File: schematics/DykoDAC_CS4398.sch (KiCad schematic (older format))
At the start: 14 parts, among them U7 CS4398

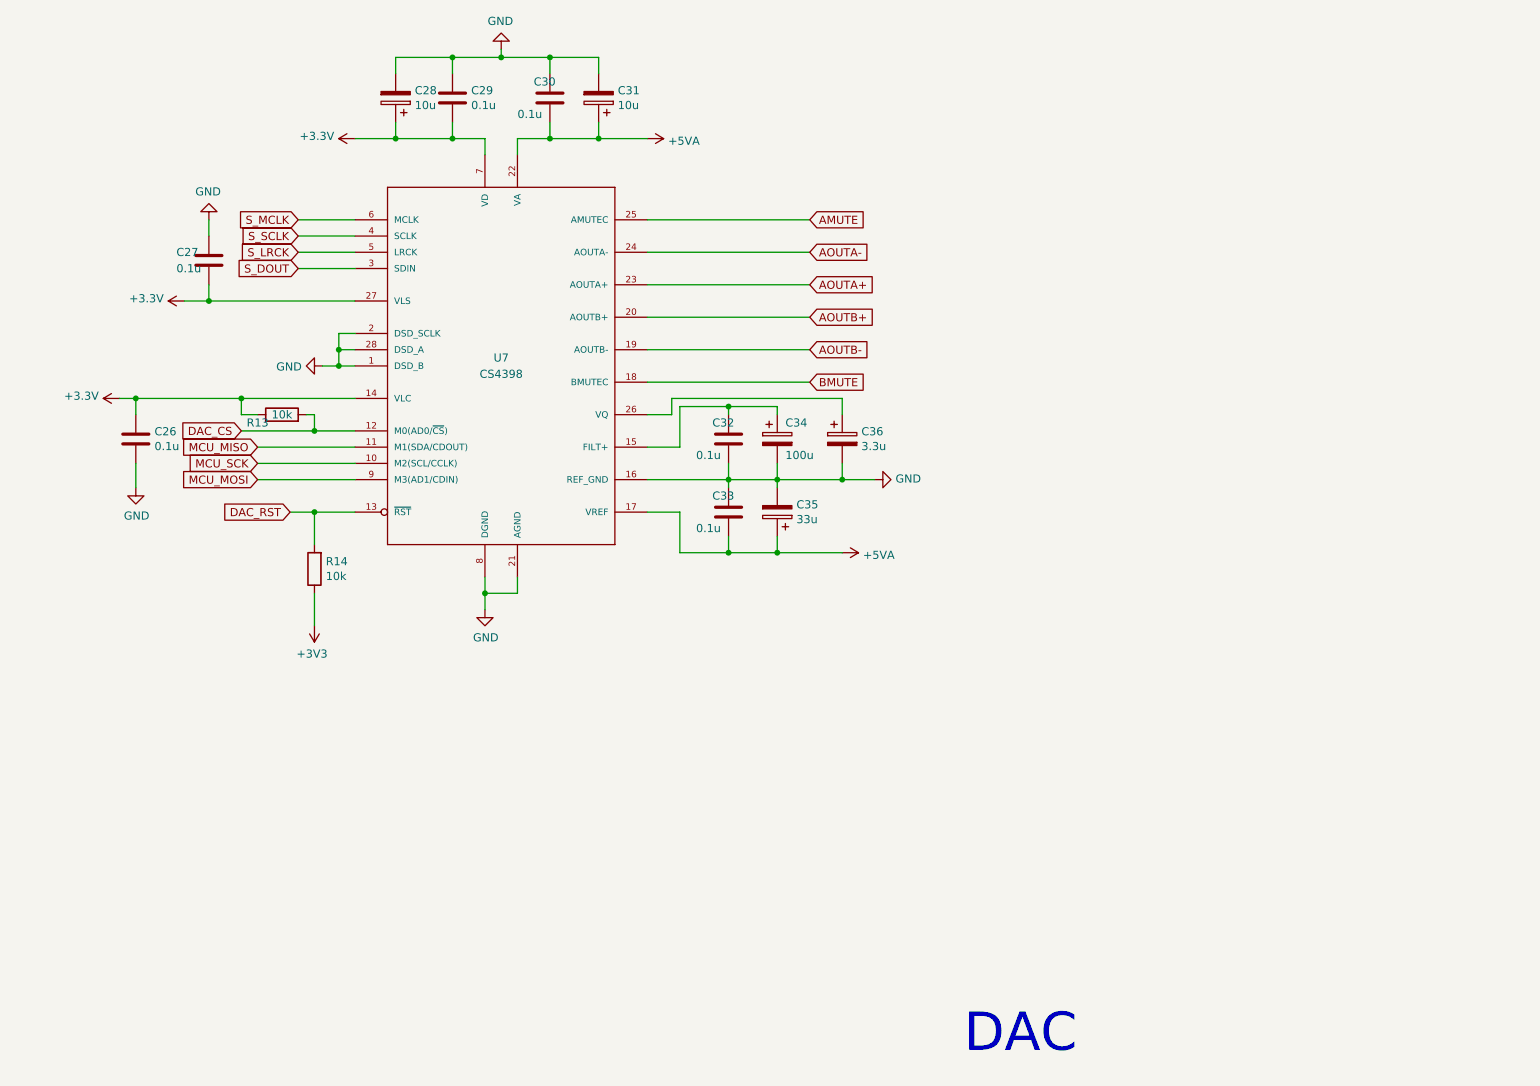
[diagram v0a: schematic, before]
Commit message: mcu input and usb added, oscilators moved to DAC schematics
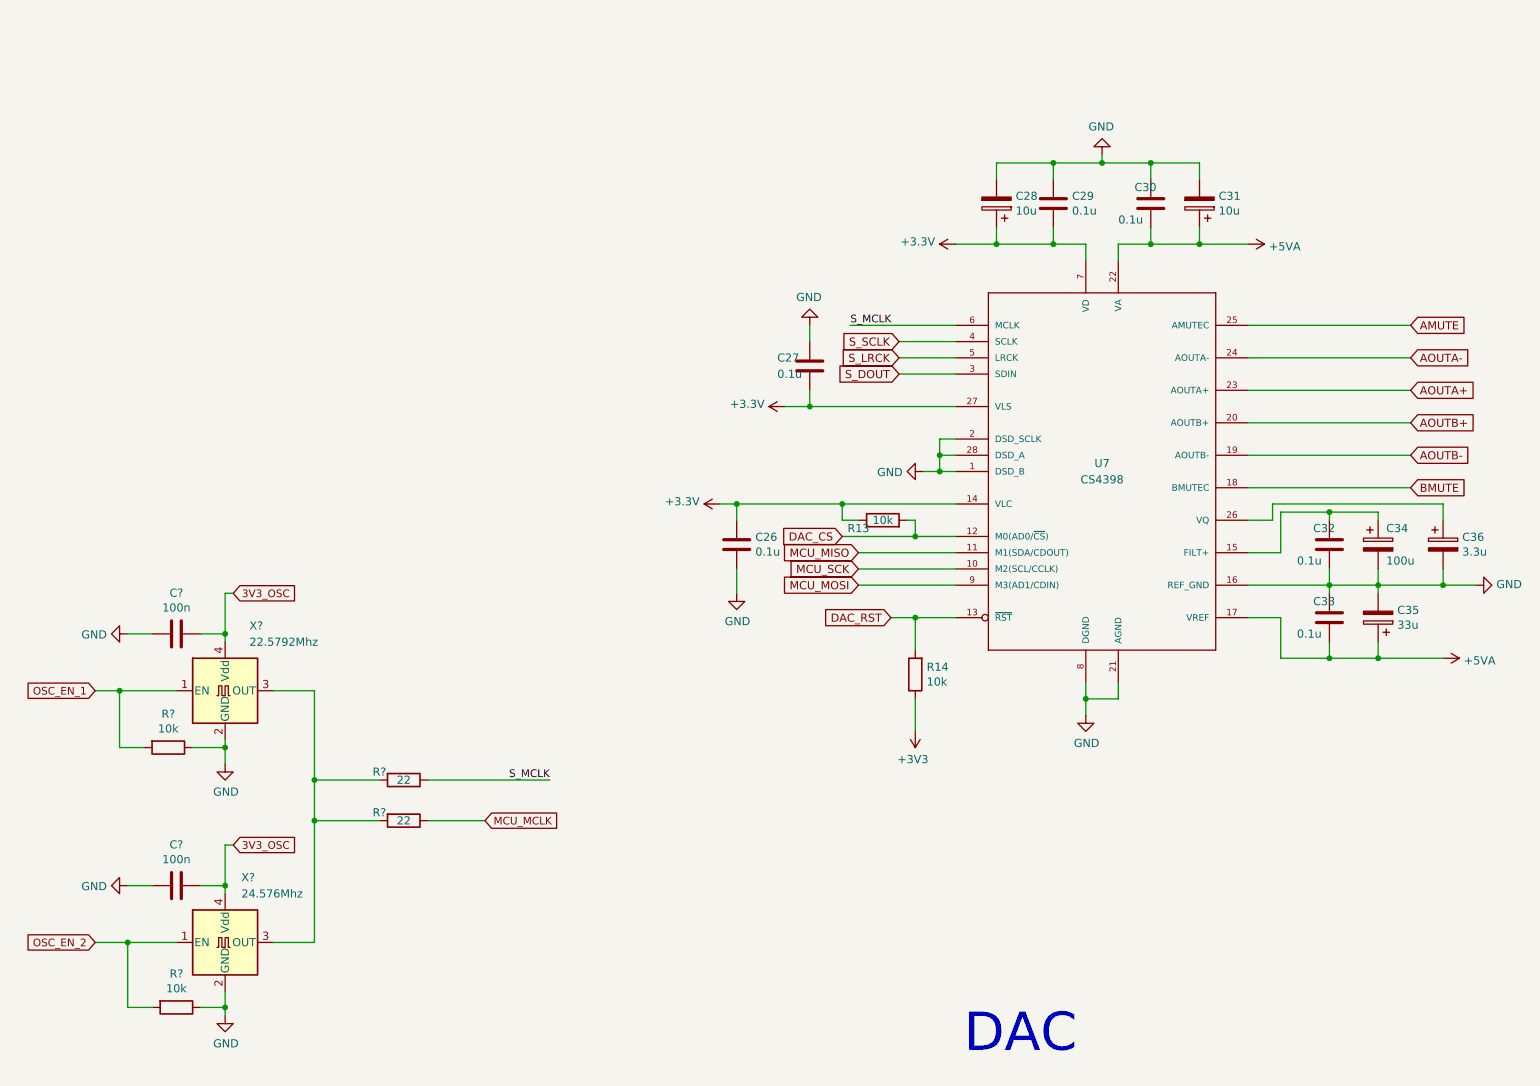
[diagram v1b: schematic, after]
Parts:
- added C? (x2): 100n, symbol Device:C
- added R? (x2): 22, symbol Device:R
- added R? (x2): 10k, symbol Device:R
- added X?: 22.5792Mhz, Oscillator:Oscillator_SMD_TXC_7C-4Pin_5.0x3.2mm, symbol Oscillator:TXC-7C
- added X?: 24.576Mhz, Oscillator:Oscillator_SMD_TXC_7C-4Pin_5.0x3.2mm, symbol Oscillator:TXC-7C
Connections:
- net GND: now also C?.2, C?.2, R?.1, R?.1, X?.2 (GND), X?.2 (GND)
- net S_MCLK: now also R?.1
- new net: R?.2, R?.2, X?.3 (OUT), X?.3 (OUT)
- new net 3V3_OSC: C?.1, C?.1, X?.4 (Vdd), X?.4 (Vdd)
- new net MCU_MCLK: R?.1
- new net OSC_EN_1: R?.2, X?.1 (EN)
- new net OSC_EN_2: R?.2, X?.1 (EN)
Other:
- moved on the sheet: C26, C27, C28, C29, C30, C31, C32, C33, C34, C35, C36, R13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

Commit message: finishing
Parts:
- C22, C23: renamed from C?; footprint (none) -> Capacitors_SMD:C_1206
- C24: renamed from C26; footprint (none) -> Capacitors_SMD:C_1206
- C25: renamed from C27; footprint (none) -> Capacitors_SMD:C_1206
- C26: renamed from C28; footprint (none) -> Capacitors_SMD:C_1206
- C27: renamed from C29; footprint (none) -> Capacitors_SMD:C_1206
- C28: renamed from C30; footprint (none) -> Capacitors_SMD:C_1206
- C29: renamed from C31; footprint (none) -> Capacitors_SMD:C_1206
- C30: renamed from C32; footprint (none) -> Capacitors_SMD:C_1206
- C31: renamed from C33; footprint (none) -> Capacitors_SMD:C_1206
- C32: renamed from C34; footprint (none) -> Capacitors_SMD:C_1206
- C33: renamed from C35; footprint (none) -> Capacitors_SMD:C_1206
- C34: renamed from C36; footprint (none) -> Capacitors_SMD:C_1206
- R1, R2, R3, R4: renamed from R?; footprint (none) -> Resistors_SMD:R_1206
- R5: renamed from R13; footprint (none) -> Resistors_SMD:R_1206
- R6: renamed from R14; footprint (none) -> Resistors_SMD:R_1206
- X1, X2: renamed from X?; footprint Oscillator:Oscillator_SMD_TXC_7C-4Pin_5.0x3.2mm -> Oscillators:Oscillator_SMD_TXC_7C-4pin_5.0x3.2mm_HandSoldering
- renumbered U7 to U8
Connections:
- net AMUTE: no longer names the net of U8.25 (AMUTEC)
- net BMUTE: no longer names the net of U8.18 (BMUTEC)
- no-connect marks 0 -> 2

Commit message: changed filter values started with PCB design
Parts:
- U8: footprint cirrus-2-TSSOP28L -> Housings_SSOP:TSSOP-28_4.4x9.7mm_Pitch0.65mm
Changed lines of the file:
@@
 F 0 "U8" H 8050 3400 50  0000 C CNN
 F 1 "CS4398" H 8050 3300 50  0000 C CNN
-F 2 "cirrus-2-TSSOP28L" H 8050 3500 50  0001 C CNN
+F 2 "Housings_SSOP:TSSOP-28_4.4x9.7mm_Pitch0.65mm" H 8050 3500 50  0001 C CNN
 F 3 "" H 8050 3350 50  0001 C CNN
 	1    8050 3350

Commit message: lots of stuf ....
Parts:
- C22, C23, C24, C25, C26, C27, C28, C29, C30, C31, C32, C33, C34: footprint Capacitors_SMD:C_1206 -> Capacitors_SMD:C_0603_HandSoldering
- R1, R2, R3, R4, R5, R6: footprint Resistors_SMD:R_1206 -> Resistors_SMD:R_0603_HandSoldering
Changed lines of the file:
@@
 F 0 "C27" H 7635 1654 50  0000 R CNN
 F 1 "0.1u" H 7635 1745 50  0000 R CNN
-F 2 "Capacitors_SMD:C_1206" H 7788 1550 50  0001 C CNN
+F 2 "Capacitors_SMD:C_0603_HandSoldering" H 7788 1550 50  0001 C CNN
 F 3 "~" H 7750 1700 50  0001 C CNN
 	1    7750 1700
@@
 F 0 "C28" H 8100 1750 50  0000 L CNN
 F 1 "0.1u" H 8100 1650 50  0000 L CNN
-F 2 "Capacitors_SMD:C_1206" H 8388 1550 50  0001 C CNN
+F 2 "Capacitors_SMD:C_0603_HandSoldering" H 8388 1550 50  0001 C CNN
 F 3 "~" H 8350 1700 50  0001 C CNN
 	1    8350 1700
@@
 F 0 "C26" H 7282 1654 50  0000 R CNN
 F 1 "10u" H 7282 1745 50  0000 R CNN
-F 2 "Capacitors_SMD:C_1206" H 7438 1550 50  0001 C CNN
+F 2 "Capacitors_SMD:C_0603_HandSoldering" H 7438 1550 50  0001 C CNN
 F 3 "~" H 7400 1700 50  0001 C CNN
 	1    7400 1700
@@
 F 0 "C29" H 8532 1654 50  0000 R CNN
 F 1 "10u" H 8532 1745 50  0000 R CNN
-F 2 "Capacitors_SMD:C_1206" H 8688 1550 50  0001 C CNN
+F 2 "Capacitors_SMD:C_0603_HandSoldering" H 8688 1550 50  0001 C CNN
 F 3 "~" H 8650 1700 50  0001 C CNN
 	1    8650 1700
@@
 F 0 "C30" H 9200 3850 50  0000 L CNN
 F 1 "0.1u" H 9200 3750 50  0000 L CNN
-F 2 "Capacitors_SMD:C_1206" H 9488 3650 50  0001 C CNN
+F 2 "Capacitors_SMD:C_0603_HandSoldering" H 9488 3650 50  0001 C CNN
 F 3 "~" H 9450 3800 50  0001 C CNN
 	1    9450 3800
@@
 F 0 "C32" H 9800 3900 50  0000 L CNN
 F 1 "100u" H 9800 3700 50  0000 L CNN
-F 2 "Capacitors_SMD:C_1206" H 9788 3650 50  0001 C CNN
+F 2 "Capacitors_SMD:C_0603_HandSoldering" H 9788 3650 50  0001 C CNN
 F 3 "~" H 9750 3800 50  0001 C CNN
 	1    9750 3800
@@
 F 0 "C31" H 9200 4300 50  0000 L CNN
 F 1 "0.1u" H 9200 4200 50  0000 L CNN
-F 2 "Capacitors_SMD:C_1206" H 9488 4100 50  0001 C CNN
+F 2 "Capacitors_SMD:C_0603_HandSoldering" H 9488 4100 50  0001 C CNN
 F 3 "~" H 9450 4250 50  0001 C CNN
 	1    9450 4250
@@
 F 0 "C33" H 9632 4204 50  0000 R CNN
 F 1 "33u" H 9632 4295 50  0000 R CNN
-F 2 "Capacitors_SMD:C_1206" H 9788 4100 50  0001 C CNN
+F 2 "Capacitors_SMD:C_0603_HandSoldering" H 9788 4100 50  0001 C CNN
 F 3 "~" H 9750 4250 50  0001 C CNN
 	1    9750 4250
@@
 F 0 "C34" H 10268 3846 50  0000 L CNN
 F 1 "3.3u" H 10268 3755 50  0000 L CNN
-F 2 "Capacitors_SMD:C_1206" H 10188 3650 50  0001 C CNN
+F 2 "Capacitors_SMD:C_0603_HandSoldering" H 10188 3650 50  0001 C CNN
 F 3 "~" H 10150 3800 50  0001 C CNN
 	1    10150 3800
@@
 F 0 "C25" H 6550 2650 50  0000 R CNN
 F 1 "0.1u" H 6550 2750 50  0000 R CNN
-F 2 "Capacitors_SMD:C_1206" H 6288 2550 50  0001 C CNN
+F 2 "Capacitors_SMD:C_0603_HandSoldering" H 6288 2550 50  0001 C CNN
 F 3 "~" H 6250 2700 50  0001 C CNN
 	1    6250 2700
@@
 F 0 "C24" H 5900 3850 50  0000 L CNN
 F 1 "0.1u" H 5915 3755 50  0000 L CNN
-F 2 "Capacitors_SMD:C_1206" H 5838 3650 50  0001 C CNN
+F 2 "Capacitors_SMD:C_0603_HandSoldering" H 5838 3650 50  0001 C CNN
 F 3 "~" H 5800 3800 50  0001 C CNN
 	1    5800 3800
@@
 F 0 "R6" H 6830 4554 50  0000 R CNN
 F 1 "10k" H 6830 4645 50  0000 R CNN
-F 2 "Resistors_SMD:R_1206" V 6830 4600 50  0001 C CNN
+F 2 "Resistors_SMD:R_0603_HandSoldering" V 6830 4600 50  0001 C CNN
 F 3 "~" H 6900 4600 50  0001 C CNN
 	1    6900 4600
@@
 F 0 "R5" V 6650 3800 50  0000 C CNN
 F 1 "10k" V 6700 3650 50  0000 C CNN
-F 2 "Resistors_SMD:R_1206" V 6630 3650 50  0001 C CNN
+F 2 "Resistors_SMD:R_0603_HandSoldering" V 6630 3650 50  0001 C CNN
 F 3 "~" H 6700 3650 50  0001 C CNN
 	1    6700 3650
@@
 F 0 "R4" V 3700 5350 50  0000 C CNN
 F 1 "22" V 3750 5500 50  0000 C CNN
-F 2 "Resistors_SMD:R_1206" V 3680 5500 50  0001 C CNN
+F 2 "Resistors_SMD:R_0603_HandSoldering" V 3680 5500 50  0001 C CNN
 F 3 "~" H 3750 5500 50  0001 C CNN
 	1    3750 5500
@@
 F 0 "R1" V 2093 5050 50  0000 C CNN
 F 1 "10k" V 2184 5050 50  0000 C CNN
-F 2 "Resistors_SMD:R_1206" V 2230 5050 50  0001 C CNN
+F 2 "Resistors_SMD:R_0603_HandSoldering" V 2230 5050 50  0001 C CNN
 F 3 "~" H 2300 5050 50  0001 C CNN
 	1    2300 5050
@@
 F 0 "R2" V 2143 6650 50  0000 C CNN
 F 1 "10k" V 2234 6650 50  0000 C CNN
-F 2 "Resistors_SMD:R_1206" V 2280 6650 50  0001 C CNN
+F 2 "Resistors_SMD:R_0603_HandSoldering" V 2280 6650 50  0001 C CNN
 F 3 "~" H 2350 6650 50  0001 C CNN
 	1    2350 6650
@@
 F 0 "C23" V 2098 5900 50  0000 C CNN
 F 1 "100n" V 2189 5900 50  0000 C CNN
-F 2 "Capacitors_SMD:C_1206" H 2388 5750 50  0001 C CNN
+F 2 "Capacitors_SMD:C_0603_HandSoldering" H 2388 5750 50  0001 C CNN
 F 3 "~" H 2350 5900 50  0001 C CNN
 	1    2350 5900
@@
 F 0 "C22" V 2098 4350 50  0000 C CNN
 F 1 "100n" V 2189 4350 50  0000 C CNN
-F 2 "Capacitors_SMD:C_1206" H 2388 4200 50  0001 C CNN
+F 2 "Capacitors_SMD:C_0603_HandSoldering" H 2388 4200 50  0001 C CNN
 F 3 "~" H 2350 4350 50  0001 C CNN
 	1    2350 4350
@@
 F 0 "R3" V 3700 5100 50  0000 C CNN
 F 1 "22" V 3750 5250 50  0000 C CNN
-F 2 "Resistors_SMD:R_1206" V 3680 5250 50  0001 C CNN
+F 2 "Resistors_SMD:R_0603_HandSoldering" V 3680 5250 50  0001 C CNN
 F 3 "~" H 3750 5250 50  0001 C CNN
 	1    3750 5250

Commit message: no message
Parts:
- C22, C23, C24, C25, C27, C28, C30, C31: footprint Capacitors_SMD:C_0603_HandSoldering -> Capacitors_SMD:C_0603
- C26, C29, C33, C34: footprint Capacitors_SMD:C_0603_HandSoldering -> Capacitors_SMD:CP_Elec_4x5.7
- C32: footprint Capacitors_SMD:C_0603_HandSoldering -> Capacitors_SMD:CP_Elec_6.3x5.8
- R1, R2, R3, R4, R5, R6: footprint Resistors_SMD:R_0603_HandSoldering -> Resistors_SMD:R_0603
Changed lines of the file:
@@
 EESchema Schematic File Version 4
-LIBS:DykoDAC-cache
-EELAYER 29 0
+EELAYER 30 0
 EELAYER END
 $Descr A4 11693 8268
@@
 F 0 "C27" H 7635 1654 50  0000 R CNN
 F 1 "0.1u" H 7635 1745 50  0000 R CNN
-F 2 "Capacitors_SMD:C_0603_HandSoldering" H 7788 1550 50  0001 C CNN
+F 2 "Capacitors_SMD:C_0603" H 7788 1550 50  0001 C CNN
 F 3 "~" H 7750 1700 50  0001 C CNN
 	1    7750 1700
@@
 F 0 "C28" H 8100 1750 50  0000 L CNN
 F 1 "0.1u" H 8100 1650 50  0000 L CNN
-F 2 "Capacitors_SMD:C_0603_HandSoldering" H 8388 1550 50  0001 C CNN
+F 2 "Capacitors_SMD:C_0603" H 8388 1550 50  0001 C CNN
 F 3 "~" H 8350 1700 50  0001 C CNN
 	1    8350 1700
@@
 F 0 "C26" H 7282 1654 50  0000 R CNN
 F 1 "10u" H 7282 1745 50  0000 R CNN
-F 2 "Capacitors_SMD:C_0603_HandSoldering" H 7438 1550 50  0001 C CNN
+F 2 "Capacitors_SMD:CP_Elec_4x5.7" H 7438 1550 50  0001 C CNN
 F 3 "~" H 7400 1700 50  0001 C CNN
 	1    7400 1700
@@
 F 0 "C29" H 8532 1654 50  0000 R CNN
 F 1 "10u" H 8532 1745 50  0000 R CNN
-F 2 "Capacitors_SMD:C_0603_HandSoldering" H 8688 1550 50  0001 C CNN
+F 2 "Capacitors_SMD:CP_Elec_4x5.7" H 8688 1550 50  0001 C CNN
 F 3 "~" H 8650 1700 50  0001 C CNN
 	1    8650 1700
@@
 F 0 "C30" H 9200 3850 50  0000 L CNN
 F 1 "0.1u" H 9200 3750 50  0000 L CNN
-F 2 "Capacitors_SMD:C_0603_HandSoldering" H 9488 3650 50  0001 C CNN
+F 2 "Capacitors_SMD:C_0603" H 9488 3650 50  0001 C CNN
 F 3 "~" H 9450 3800 50  0001 C CNN
 	1    9450 3800
@@
 F 0 "C32" H 9800 3900 50  0000 L CNN
 F 1 "100u" H 9800 3700 50  0000 L CNN
-F 2 "Capacitors_SMD:C_0603_HandSoldering" H 9788 3650 50  0001 C CNN
+F 2 "Capacitors_SMD:CP_Elec_6.3x5.8" H 9788 3650 50  0001 C CNN
 F 3 "~" H 9750 3800 50  0001 C CNN
 	1    9750 3800
@@
 F 0 "C31" H 9200 4300 50  0000 L CNN
 F 1 "0.1u" H 9200 4200 50  0000 L CNN
-F 2 "Capacitors_SMD:C_0603_HandSoldering" H 9488 4100 50  0001 C CNN
+F 2 "Capacitors_SMD:C_0603" H 9488 4100 50  0001 C CNN
 F 3 "~" H 9450 4250 50  0001 C CNN
 	1    9450 4250
@@
 F 0 "C33" H 9632 4204 50  0000 R CNN
 F 1 "33u" H 9632 4295 50  0000 R CNN
-F 2 "Capacitors_SMD:C_0603_HandSoldering" H 9788 4100 50  0001 C CNN
+F 2 "Capacitors_SMD:CP_Elec_4x5.7" H 9788 4100 50  0001 C CNN
 F 3 "~" H 9750 4250 50  0001 C CNN
 	1    9750 4250
@@
 F 0 "C34" H 10268 3846 50  0000 L CNN
 F 1 "3.3u" H 10268 3755 50  0000 L CNN
-F 2 "Capacitors_SMD:C_0603_HandSoldering" H 10188 3650 50  0001 C CNN
+F 2 "Capacitors_SMD:CP_Elec_4x5.7" H 10188 3650 50  0001 C CNN
 F 3 "~" H 10150 3800 50  0001 C CNN
 	1    10150 3800
@@
 F 0 "C25" H 6550 2650 50  0000 R CNN
 F 1 "0.1u" H 6550 2750 50  0000 R CNN
-F 2 "Capacitors_SMD:C_0603_HandSoldering" H 6288 2550 50  0001 C CNN
+F 2 "Capacitors_SMD:C_0603" H 6288 2550 50  0001 C CNN
 F 3 "~" H 6250 2700 50  0001 C CNN
 	1    6250 2700
@@
 F 0 "C24" H 5900 3850 50  0000 L CNN
 F 1 "0.1u" H 5915 3755 50  0000 L CNN
-F 2 "Capacitors_SMD:C_0603_HandSoldering" H 5838 3650 50  0001 C CNN
+F 2 "Capacitors_SMD:C_0603" H 5838 3650 50  0001 C CNN
 F 3 "~" H 5800 3800 50  0001 C CNN
 	1    5800 3800
@@
 F 0 "R6" H 6830 4554 50  0000 R CNN
 F 1 "10k" H 6830 4645 50  0000 R CNN
-F 2 "Resistors_SMD:R_0603_HandSoldering" V 6830 4600 50  0001 C CNN
+F 2 "Resistors_SMD:R_0603" V 6830 4600 50  0001 C CNN
 F 3 "~" H 6900 4600 50  0001 C CNN
 	1    6900 4600
@@
 F 0 "R5" V 6650 3800 50  0000 C CNN
 F 1 "10k" V 6700 3650 50  0000 C CNN
-F 2 "Resistors_SMD:R_0603_HandSoldering" V 6630 3650 50  0001 C CNN
+F 2 "Resistors_SMD:R_0603" V 6630 3650 50  0001 C CNN
 F 3 "~" H 6700 3650 50  0001 C CNN
 	1    6700 3650
@@
 F 0 "R4" V 3700 5350 50  0000 C CNN
 F 1 "22" V 3750 5500 50  0000 C CNN
-F 2 "Resistors_SMD:R_0603_HandSoldering" V 3680 5500 50  0001 C CNN
+F 2 "Resistors_SMD:R_0603" V 3680 5500 50  0001 C CNN
 F 3 "~" H 3750 5500 50  0001 C CNN
 	1    3750 5500
@@
 F 0 "R1" V 2093 5050 50  0000 C CNN
 F 1 "10k" V 2184 5050 50  0000 C CNN
-F 2 "Resistors_SMD:R_0603_HandSoldering" V 2230 5050 50  0001 C CNN
+F 2 "Resistors_SMD:R_0603" V 2230 5050 50  0001 C CNN
 F 3 "~" H 2300 5050 50  0001 C CNN
 	1    2300 5050
@@
 F 0 "R2" V 2143 6650 50  0000 C CNN
 F 1 "10k" V 2234 6650 50  0000 C CNN
-F 2 "Resistors_SMD:R_0603_HandSoldering" V 2280 6650 50  0001 C CNN
+F 2 "Resistors_SMD:R_0603" V 2280 6650 50  0001 C CNN
 F 3 "~" H 2350 6650 50  0001 C CNN
 	1    2350 6650
@@
 F 0 "C23" V 2098 5900 50  0000 C CNN
 F 1 "100n" V 2189 5900 50  0000 C CNN
-F 2 "Capacitors_SMD:C_0603_HandSoldering" H 2388 5750 50  0001 C CNN
+F 2 "Capacitors_SMD:C_0603" H 2388 5750 50  0001 C CNN
 F 3 "~" H 2350 5900 50  0001 C CNN
 	1    2350 5900
@@
 F 0 "C22" V 2098 4350 50  0000 C CNN
 F 1 "100n" V 2189 4350 50  0000 C CNN
-F 2 "Capacitors_SMD:C_0603_HandSoldering" H 2388 4200 50  0001 C CNN
+F 2 "Capacitors_SMD:C_0603" H 2388 4200 50  0001 C CNN
 F 3 "~" H 2350 4350 50  0001 C CNN
 	1    2350 4350
@@
 F 0 "R3" V 3700 5100 50  0000 C CNN
 F 1 "22" V 3750 5250 50  0000 C CNN
-F 2 "Resistors_SMD:R_0603_HandSoldering" V 3680 5250 50  0001 C CNN
+F 2 "Resistors_SMD:R_0603" V 3680 5250 50  0001 C CNN
 F 3 "~" H 3750 5250 50  0001 C CNN
 	1    3750 5250
